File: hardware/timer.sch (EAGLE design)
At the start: 50 parts, among them J1 DCJ0202, Q1 AO3400, U1 MC34063D, U2 STM8SX03F3, U3 NC-78LACU05, X1 12MHz

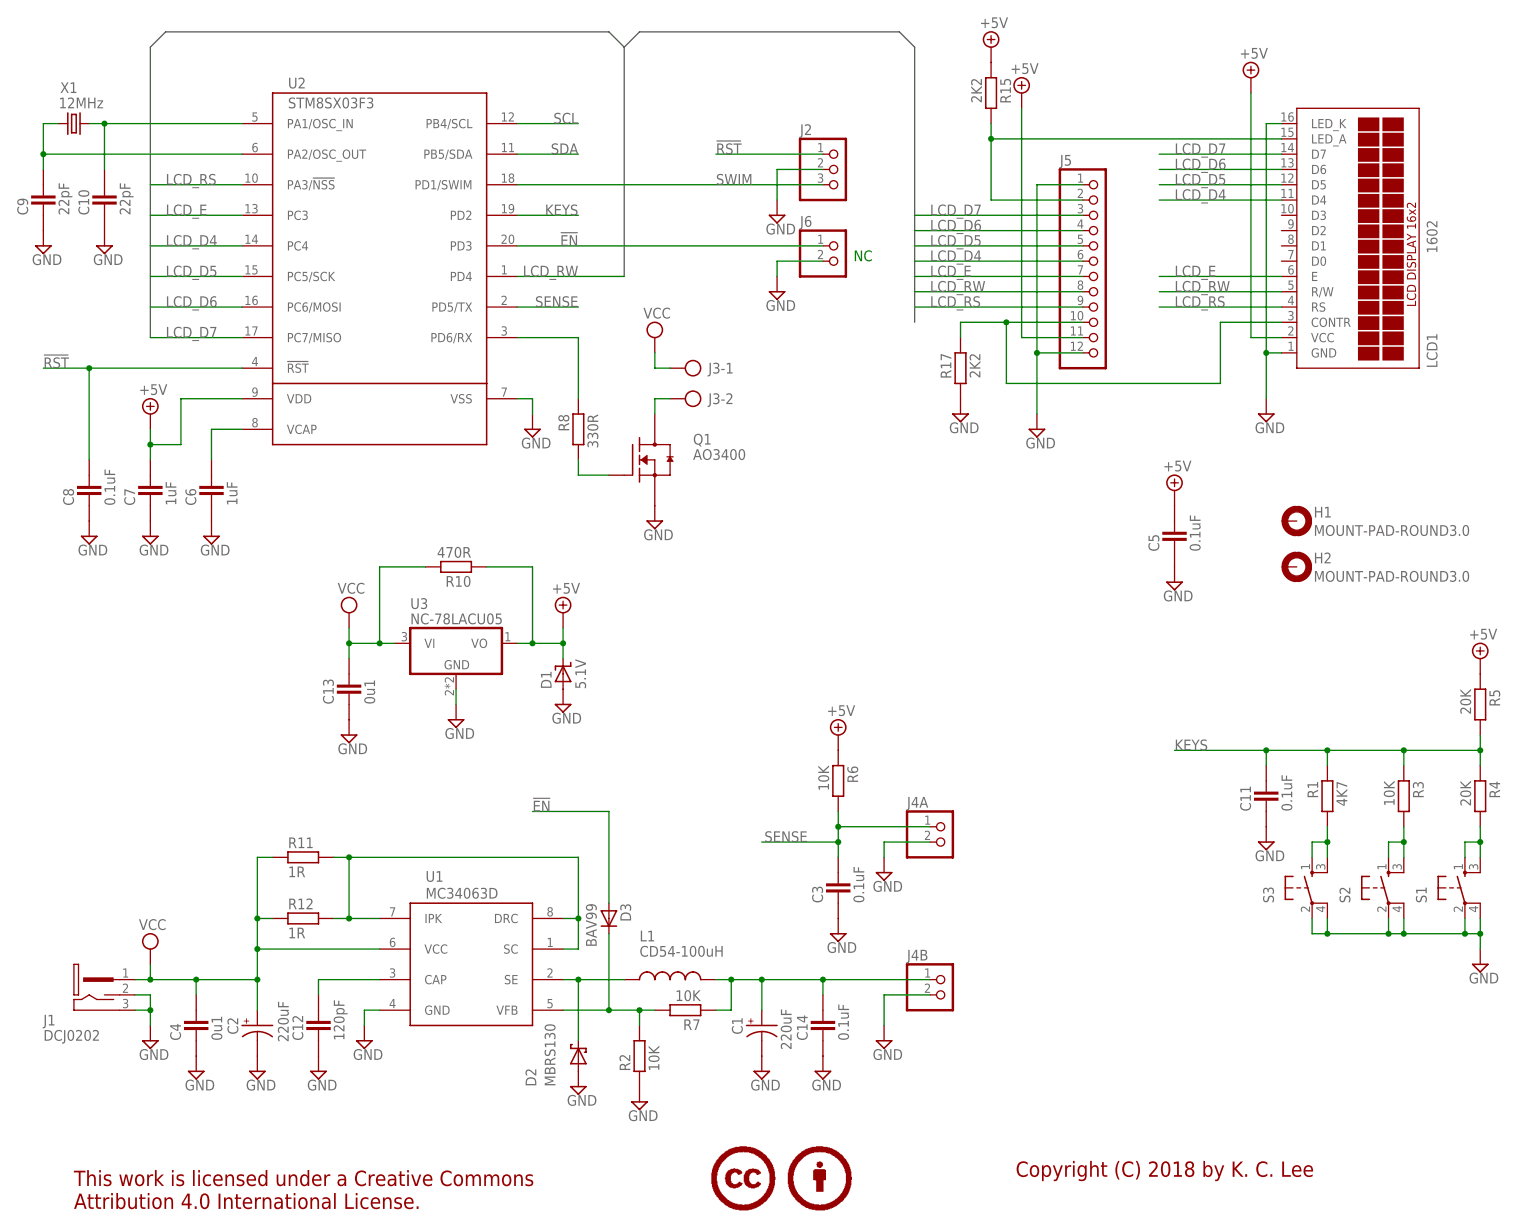
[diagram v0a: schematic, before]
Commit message: Servo support + alarm remainder time
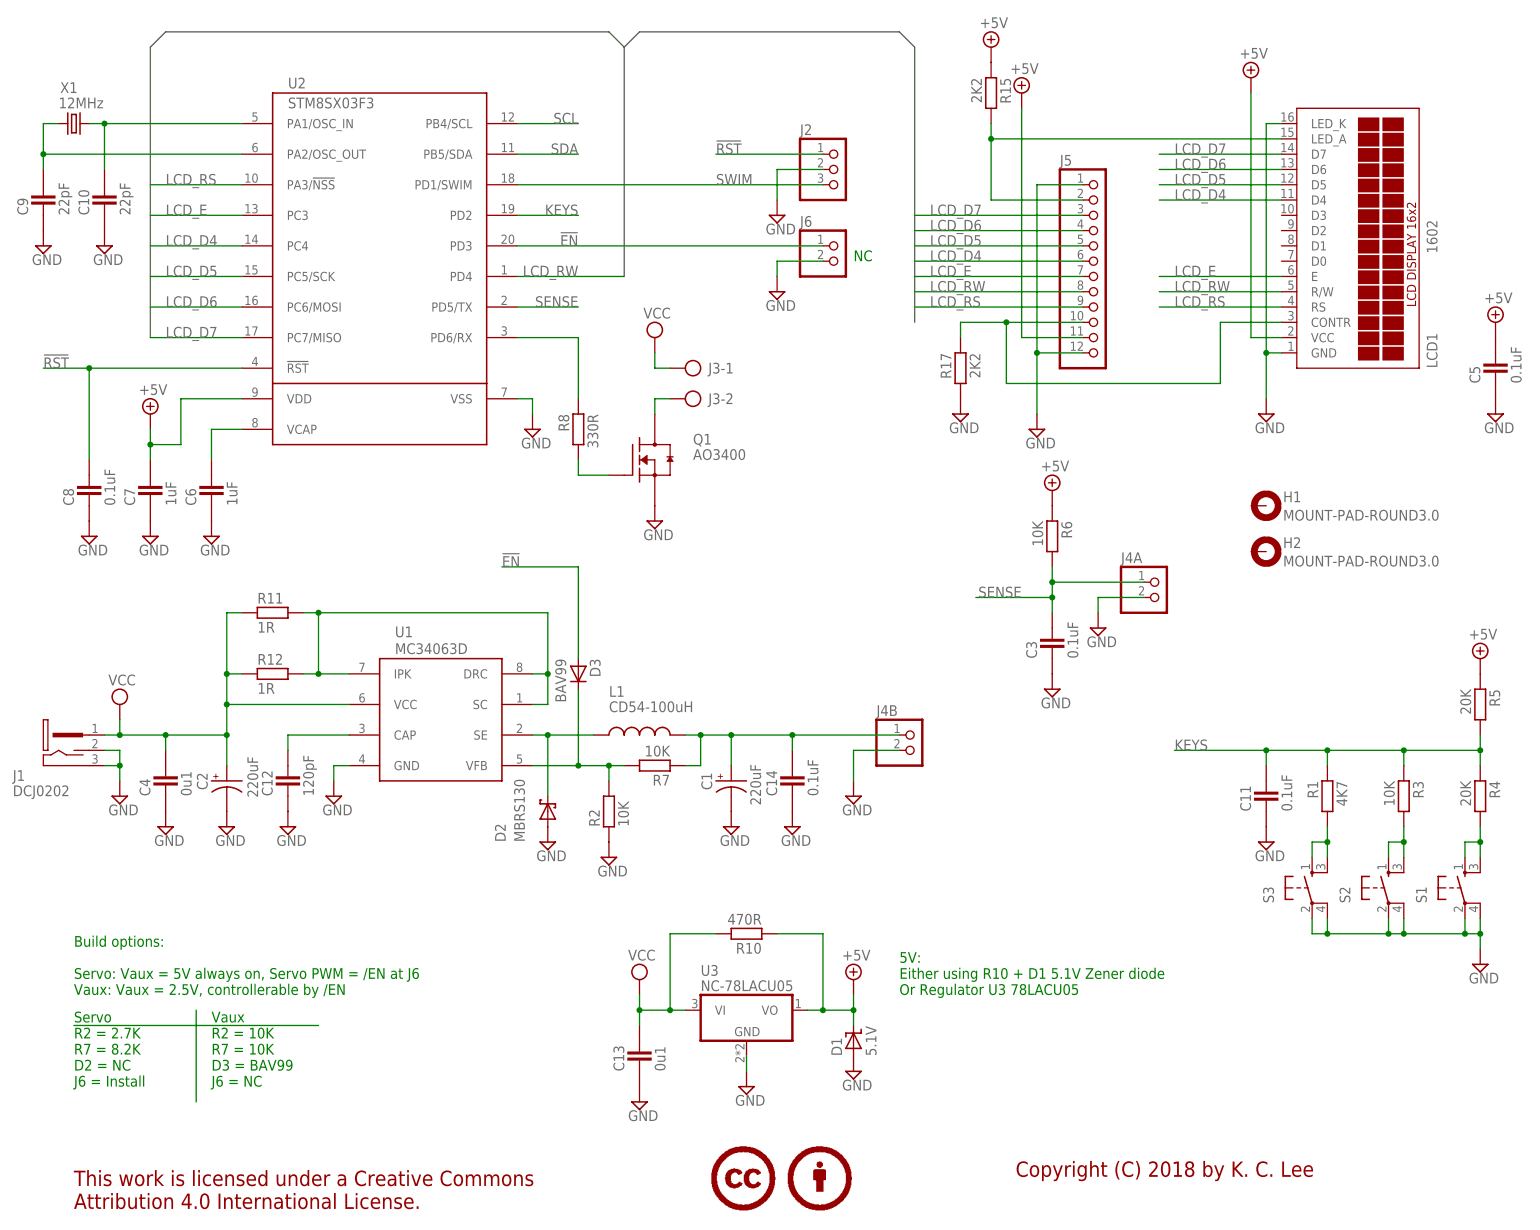
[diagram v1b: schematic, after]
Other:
- note added: "5V: Either using R10 + D1 5.1V Zener diode Or Regulator U3 78LACU05"
- note added: "Build options: Servo: Vaux = 5V always on, Servo PWM = /EN at J6 Vaux: Vaux = 2.5V, controllerable by /EN"
- note added: "Servo R2 = 2.7K R7 = 8.2K D2 = NC J6 = Install"
- note added: "Vaux R2 = 10K R7 = 10K D3 = BAV99 J6 = NC"
- moved on the sheet: C1, C12, C13, C14, C2, C3, C4, C5, D1, D2, D3, H1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
